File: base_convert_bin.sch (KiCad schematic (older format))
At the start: 27 parts, among them Q2 Q_PNP_BEC, Q3 Q_PNP_BEC, Q4 Q_PNP_BEC, Q5 Q_PNP_BEC, Q6 Q_NPN_BEC, Q7 Q_NPN_BEC, Q8 Q_NPN_BEC, Q9 Q_NPN_BEC

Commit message: correct LED part numbers
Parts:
- D10: Mfg Part Number 150080RS75001 -> 150080RS75000
- D11: Mfg Part Number 150080RS75002 -> 150080RS75000
- D12: Mfg Part Number 150080RS75003 -> 150080RS75000
- D13: Mfg Part Number 150080RS75004 -> 150080RS75000
- D14: Mfg Part Number 150080RS75005 -> 150080RS75000
- D15: Mfg Part Number 150080RS75006 -> 150080RS75000
- D16: Mfg Part Number 150080RS75007 -> 150080RS75000
- D2: Mfg Part Number 150080RS75008 -> 150080RS75000
- D3: Mfg Part Number 150080RS75009 -> 150080RS75000
- D4: Mfg Part Number 150080RS75010 -> 150080RS75000
- D5: Mfg Part Number 150080RS75011 -> 150080RS75000
- D6: Mfg Part Number 150080RS75012 -> 150080RS75000
- D7: Mfg Part Number 150080RS75013 -> 150080RS75000
- D8: Mfg Part Number 150080RS75014 -> 150080RS75000
- D9: Mfg Part Number 150080RS75015 -> 150080RS75000
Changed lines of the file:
@@
 F 4 "LED RED CLEAR 0805 SMD" H 5200 1750 50  0001 C CNN "Description"
 F 5 "Wurth Electronics Inc." H 5200 1750 50  0001 C CNN "Manufacture"
-F 6 "150080RS75004" H 5200 1750 50  0001 C CNN "Mfg Part Number"
+F 6 "150080RS75000" H 5200 1750 50  0001 C CNN "Mfg Part Number"
 F 7 "0805" H 5200 1750 50  0001 C CNN "Package"
 	1    5200 1550
@@
 F 4 "LED RED CLEAR 0805 SMD" H 4900 1750 50  0001 C CNN "Description"
 F 5 "Wurth Electronics Inc." H 4900 1750 50  0001 C CNN "Manufacture"
-F 6 "150080RS75015" H 4900 1750 50  0001 C CNN "Mfg Part Number"
+F 6 "150080RS75000" H 4900 1750 50  0001 C CNN "Mfg Part Number"
 F 7 "0805" H 4900 1750 50  0001 C CNN "Package"
 	1    4900 1550
@@
 F 4 "LED RED CLEAR 0805 SMD" H 4600 1750 50  0001 C CNN "Description"
 F 5 "Wurth Electronics Inc." H 4600 1750 50  0001 C CNN "Manufacture"
-F 6 "150080RS75011" H 4600 1750 50  0001 C CNN "Mfg Part Number"
+F 6 "150080RS75000" H 4600 1750 50  0001 C CNN "Mfg Part Number"
 F 7 "0805" H 4600 1750 50  0001 C CNN "Package"
 	1    4600 1550
@@
 F 4 "LED RED CLEAR 0805 SMD" H 5200 3400 50  0001 C CNN "Description"
 F 5 "Wurth Electronics Inc." H 5200 3400 50  0001 C CNN "Manufacture"
-F 6 "150080RS75005" H 5200 3400 50  0001 C CNN "Mfg Part Number"
+F 6 "150080RS75000" H 5200 3400 50  0001 C CNN "Mfg Part Number"
 F 7 "0805" H 5200 3400 50  0001 C CNN "Package"
 	1    5200 3200
@@
 F 4 "LED RED CLEAR 0805 SMD" H 4900 3400 50  0001 C CNN "Description"
 F 5 "Wurth Electronics Inc." H 4900 3400 50  0001 C CNN "Manufacture"
-F 6 "150080RS75001" H 4900 3400 50  0001 C CNN "Mfg Part Number"
+F 6 "150080RS75000" H 4900 3400 50  0001 C CNN "Mfg Part Number"
 F 7 "0805" H 4900 3400 50  0001 C CNN "Package"
 	1    4900 3200
@@
 F 4 "LED RED CLEAR 0805 SMD" H 4600 3400 50  0001 C CNN "Description"
 F 5 "Wurth Electronics Inc." H 4600 3400 50  0001 C CNN "Manufacture"
-F 6 "150080RS75012" H 4600 3400 50  0001 C CNN "Mfg Part Number"
+F 6 "150080RS75000" H 4600 3400 50  0001 C CNN "Mfg Part Number"
 F 7 "0805" H 4600 3400 50  0001 C CNN "Package"
 	1    4600 3200
@@
 F 4 "LED RED CLEAR 0805 SMD" H 4300 3400 50  0001 C CNN "Description"
 F 5 "Wurth Electronics Inc." H 4300 3400 50  0001 C CNN "Manufacture"
-F 6 "150080RS75008" H 4300 3400 50  0001 C CNN "Mfg Part Number"
+F 6 "150080RS75000" H 4300 3400 50  0001 C CNN "Mfg Part Number"
 F 7 "0805" H 4300 3400 50  0001 C CNN "Package"
 	1    4300 3200
@@
 F 4 "LED RED CLEAR 0805 SMD" H 5200 5100 50  0001 C CNN "Description"
 F 5 "Wurth Electronics Inc." H 5200 5100 50  0001 C CNN "Manufacture"
-F 6 "150080RS75006" H 5200 5100 50  0001 C CNN "Mfg Part Number"
+F 6 "150080RS75000" H 5200 5100 50  0001 C CNN "Mfg Part Number"
 F 7 "0805" H 5200 5100 50  0001 C CNN "Package"
 	1    5200 4900
@@
 F 4 "LED RED CLEAR 0805 SMD" H 4900 5100 50  0001 C CNN "Description"
 F 5 "Wurth Electronics Inc." H 4900 5100 50  0001 C CNN "Manufacture"
-F 6 "150080RS75002" H 4900 5100 50  0001 C CNN "Mfg Part Number"
+F 6 "150080RS75000" H 4900 5100 50  0001 C CNN "Mfg Part Number"
 F 7 "0805" H 4900 5100 50  0001 C CNN "Package"
 	1    4900 4900
@@
 F 4 "LED RED CLEAR 0805 SMD" H 4600 5100 50  0001 C CNN "Description"
 F 5 "Wurth Electronics Inc." H 4600 5100 50  0001 C CNN "Manufacture"
-F 6 "150080RS75013" H 4600 5100 50  0001 C CNN "Mfg Part Number"
+F 6 "150080RS75000" H 4600 5100 50  0001 C CNN "Mfg Part Number"
 F 7 "0805" H 4600 5100 50  0001 C CNN "Package"
 	1    4600 4900
@@
 F 4 "LED RED CLEAR 0805 SMD" H 4300 5100 50  0001 C CNN "Description"
 F 5 "Wurth Electronics Inc." H 4300 5100 50  0001 C CNN "Manufacture"
-F 6 "150080RS75009" H 4300 5100 50  0001 C CNN "Mfg Part Number"
+F 6 "150080RS75000" H 4300 5100 50  0001 C CNN "Mfg Part Number"
 F 7 "0805" H 4300 5100 50  0001 C CNN "Package"
 	1    4300 4900
@@
 F 4 "LED RED CLEAR 0805 SMD" H 5200 6750 50  0001 C CNN "Description"
 F 5 "Wurth Electronics Inc." H 5200 6750 50  0001 C CNN "Manufacture"
-F 6 "150080RS75007" H 5200 6750 50  0001 C CNN "Mfg Part Number"
+F 6 "150080RS75000" H 5200 6750 50  0001 C CNN "Mfg Part Number"
 F 7 "0805" H 5200 6750 50  0001 C CNN "Package"
 	1    5200 6550
@@
 F 4 "LED RED CLEAR 0805 SMD" H 4900 6750 50  0001 C CNN "Description"
 F 5 "Wurth Electronics Inc." H 4900 6750 50  0001 C CNN "Manufacture"
-F 6 "150080RS75003" H 4900 6750 50  0001 C CNN "Mfg Part Number"
+F 6 "150080RS75000" H 4900 6750 50  0001 C CNN "Mfg Part Number"
 F 7 "0805" H 4900 6750 50  0001 C CNN "Package"
 	1    4900 6550
@@
 F 4 "LED RED CLEAR 0805 SMD" H 4600 6750 50  0001 C CNN "Description"
 F 5 "Wurth Electronics Inc." H 4600 6750 50  0001 C CNN "Manufacture"
-F 6 "150080RS75014" H 4600 6750 50  0001 C CNN "Mfg Part Number"
+F 6 "150080RS75000" H 4600 6750 50  0001 C CNN "Mfg Part Number"
 F 7 "0805" H 4600 6750 50  0001 C CNN "Package"
 	1    4600 6550
@@
 F 4 "LED RED CLEAR 0805 SMD" H 4300 6750 50  0001 C CNN "Description"
 F 5 "Wurth Electronics Inc." H 4300 6750 50  0001 C CNN "Manufacture"
-F 6 "150080RS75010" H 4300 6750 50  0001 C CNN "Mfg Part Number"
+F 6 "150080RS75000" H 4300 6750 50  0001 C CNN "Mfg Part Number"
 F 7 "0805" H 4300 6750 50  0001 C CNN "Package"
 	1    4300 6550

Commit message: update RN part numbers
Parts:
- RN1, RN3: Description RES ARRAY 4 RES 4.7K OHM 1206 -> RES ARRAY 4 RES 5.6K OHM 2012; Manufacture Stackpole Electronics Inc. -> Rohm Semiconductor; Mfg Part Number RAVF164DJT4K70 -> MNR34J5ABJ562; Package 1206 -> 2012
- RN2: Mfg Part Number MNR14ERAPJ151 -> MNR34J5ABJ151; Package 1206 -> 2012
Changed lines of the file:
@@
 F 2 "Resistors_SMD:R_Array_Convex_4x1206" V 3675 1200 50  0001 C CNN
 F 3 "https://www.seielect.com/Catalog/SEI-RAVF.pdf" H 3400 1200 50  0001 C CNN
-F 4 "Stackpole Electronics Inc." H 3400 1200 60  0001 C CNN "Manufacture"
-F 5 "RAVF164DJT4K70" H 3400 1200 60  0001 C CNN "Mfg Part Number"
-F 6 "1206" H 3400 1200 60  0001 C CNN "Package"
-F 7 "RES ARRAY 4 RES 4.7K OHM 1206" H 3400 1200 60  0001 C CNN "Description"
+F 4 "Rohm Semiconductor" H 3400 1200 60  0001 C CNN "Manufacture"
+F 5 "MNR34J5ABJ562" H 3400 1200 60  0001 C CNN "Mfg Part Number"
+F 6 "2012" H 3400 1200 60  0001 C CNN "Package"
+F 7 "RES ARRAY 4 RES 5.6K OHM 2012" H 3400 1200 60  0001 C CNN "Description"
 	1    3400 1200
 	0    -1   1    0
@@
 F 2 "Resistors_SMD:R_Array_Convex_4x1206" V 10675 2350 50  0001 C CNN
 F 3 "https://www.seielect.com/Catalog/SEI-RAVF.pdf" H 10400 2350 50  0001 C CNN
-F 4 "Stackpole Electronics Inc." H 10400 2350 60  0001 C CNN "Manufacture"
-F 5 "RAVF164DJT4K70" H 10400 2350 60  0001 C CNN "Mfg Part Number"
-F 6 "1206" H 10400 2350 60  0001 C CNN "Package"
-F 7 "RES ARRAY 4 RES 4.7K OHM 1206" H 10400 2350 60  0001 C CNN "Description"
+F 4 "Rohm Semiconductor" H 10400 2350 60  0001 C CNN "Manufacture"
+F 5 "MNR34J5ABJ562" H 10400 2350 60  0001 C CNN "Mfg Part Number"
+F 6 "2012" H 10400 2350 60  0001 C CNN "Package"
+F 7 "RES ARRAY 4 RES 5.6K OHM 2012" H 10400 2350 60  0001 C CNN "Description"
 	1    10400 2350
 	0    1    1    0
@@
 F 3 "http://rohmfs.rohm.com/en/products/databook/datasheet/passive/resistor/chip_resistor_network/mnr_g.pdf" H 8200 1700 50  0001 C CNN
 F 4 "Rohm Semiconductor" H 8200 1700 60  0001 C CNN "Manufacture"
-F 5 "MNR14ERAPJ151" H 8200 1700 60  0001 C CNN "Mfg Part Number"
-F 6 "1206" H 8200 1700 60  0001 C CNN "Package"
+F 5 "MNR34J5ABJ151" H 8200 1700 60  0001 C CNN "Mfg Part Number"
+F 6 "2012" H 8200 1700 60  0001 C CNN "Package"
 F 7 "RES ARRAY 4 RES 150 OHM 1206" H 8200 1700 60  0001 C CNN "Description"
 	1    8200 1700

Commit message: PNP transistor change to prebiased PNP
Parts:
- Q2: Description TRANS PNP 40V 0.2A SOT23 -> TRANS PREBIAS PNP 250MW TO236AB; Mfg Part Number PMBT3906,235 -> PDTA123ET,215
- Q3: Description TRANS PNP 40V 0.2A SOT24 -> TRANS PREBIAS PNP 250MW TO236AB; Mfg Part Number PMBT3906,235 -> PDTA123ET,215
- Q4: Description TRANS PNP 40V 0.2A SOT26 -> TRANS PREBIAS PNP 250MW TO236AB; Mfg Part Number PMBT3906,235 -> PDTA123ET,215
- Q5: Description TRANS PNP 40V 0.2A SOT27 -> TRANS PREBIAS PNP 250MW TO236AB; Mfg Part Number PMBT3906,235 -> PDTA123ET,215
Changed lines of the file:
@@
 F 1 "Q_PNP_BEC" H 4400 950 50  0000 L CNN
 F 2 "TO_SOT_Packages_SMD:SOT-23" H 4400 1100 50  0001 C CNN
-F 3 "https://assets.nexperia.com/documents/data-sheet/PMBT3906.pdf" H 4200 1000 50  0001 C CNN
-F 4 "TRANS PNP 40V 0.2A SOT23" H 4400 1150 50  0001 C CNN "Description"
+F 3 "https://assets.nexperia.com/documents/data-sheet/PDTA123E_SERIES.pdf" H 4200 1000 50  0001 C CNN
+F 4 "TRANS PREBIAS PNP 250MW TO236AB" H 4400 1150 50  0001 C CNN "Description"
 F 5 "Nexperia USA Inc." H 4400 1150 50  0001 C CNN "Manufacture"
-F 6 "PMBT3906,235" H 4400 1150 50  0001 C CNN "Mfg Part Number"
+F 6 "PDTA123ET,215" H 4400 1150 50  0001 C CNN "Mfg Part Number"
 F 7 "SOT-23" H 4400 1150 50  0001 C CNN "Package"
 	1    4200 1000
@@
 F 1 "Q_PNP_BEC" H 4400 2600 50  0000 L CNN
 F 2 "TO_SOT_Packages_SMD:SOT-23" H 4400 2750 50  0001 C CNN
-F 3 "https://assets.nexperia.com/documents/data-sheet/PMBT3906.pdf" H 4200 2650 50  0001 C CNN
-F 4 "TRANS PNP 40V 0.2A SOT24" H 4400 2800 50  0001 C CNN "Description"
+F 3 "https://assets.nexperia.com/documents/data-sheet/PDTA123E_SERIES.pdf" H 4200 2650 50  0001 C CNN
+F 4 "TRANS PREBIAS PNP 250MW TO236AB" H 4400 2800 50  0001 C CNN "Description"
 F 5 "Nexperia USA Inc." H 4400 2800 50  0001 C CNN "Manufacture"
-F 6 "PMBT3906,235" H 4400 2800 50  0001 C CNN "Mfg Part Number"
+F 6 "PDTA123ET,215" H 4400 2800 50  0001 C CNN "Mfg Part Number"
 F 7 "SOT-23" H 4400 2800 50  0001 C CNN "Package"
 	1    4200 2650
@@
 F 1 "Q_PNP_BEC" H 4400 4300 50  0000 L CNN
 F 2 "TO_SOT_Packages_SMD:SOT-23" H 4400 4450 50  0001 C CNN
-F 3 "https://assets.nexperia.com/documents/data-sheet/PMBT3906.pdf" H 4200 4350 50  0001 C CNN
-F 4 "TRANS PNP 40V 0.2A SOT26" H 4400 4500 50  0001 C CNN "Description"
+F 3 "https://assets.nexperia.com/documents/data-sheet/PDTA123E_SERIES.pdf" H 4200 4350 50  0001 C CNN
+F 4 "TRANS PREBIAS PNP 250MW TO236AB" H 4400 4500 50  0001 C CNN "Description"
 F 5 "Nexperia USA Inc." H 4400 4500 50  0001 C CNN "Manufacture"
-F 6 "PMBT3906,235" H 4400 4500 50  0001 C CNN "Mfg Part Number"
+F 6 "PDTA123ET,215" H 4400 4500 50  0001 C CNN "Mfg Part Number"
 F 7 "SOT-23" H 4400 4500 50  0001 C CNN "Package"
 	1    4200 4350
@@
 F 1 "Q_PNP_BEC" H 4400 5950 50  0000 L CNN
 F 2 "TO_SOT_Packages_SMD:SOT-23" H 4400 6100 50  0001 C CNN
-F 3 "https://assets.nexperia.com/documents/data-sheet/PMBT3906.pdf" H 4200 6000 50  0001 C CNN
-F 4 "TRANS PNP 40V 0.2A SOT27" H 4400 6150 50  0001 C CNN "Description"
+F 3 "https://assets.nexperia.com/documents/data-sheet/PDTA123E_SERIES.pdf" H 4200 6000 50  0001 C CNN
+F 4 "TRANS PREBIAS PNP 250MW TO236AB" H 4400 6150 50  0001 C CNN "Description"
 F 5 "Nexperia USA Inc." H 4400 6150 50  0001 C CNN "Manufacture"
-F 6 "PMBT3906,235" H 4400 6150 50  0001 C CNN "Mfg Part Number"
+F 6 "PDTA123ET,215" H 4400 6150 50  0001 C CNN "Mfg Part Number"
 F 7 "SOT-23" H 4400 6150 50  0001 C CNN "Package"
 	1    4200 6000
@@
 	4300 750  4300 800
 Wire Wire Line
-	4300 1200 4300 1400
+	4300 1200 4300 1300
 Wire Wire Line
 	5200 1300 5200 1400
 Wire Wire Line
-	4300 1300 5200 1300
+	4300 1300 4600 1300
 Wire Wire Line
 	4900 1400 4900 1300
@@
 Wire Wire Line
 	5200 1950 5200 1700
-Wire Bus Line
-	4400 2050 5400 2050
 Wire Wire Line
 	9750 2150 10200 2150
@@
 	4300 2400 4300 2450
 Wire Wire Line
-	4300 2850 4300 3050
+	4300 2850 4300 2950
 Wire Wire Line
 	5200 2950 5200 3050
 Wire Wire Line
-	4300 2950 5200 2950
+	4300 2950 4600 2950
 Wire Wire Line
 	4900 3050 4900 2950
@@
 Wire Wire Line
 	5200 3600 5200 3350
-Wire Bus Line
-	4400 3700 5400 3700
 Wire Wire Line
 	4300 4100 4300 4150
 Wire Wire Line
-	4300 4550 4300 4750
+	4300 4550 4300 4650
 Wire Wire Line
 	5200 4650 5200 4750
 Wire Wire Line
-	4300 4650 5200 4650
+	4300 4650 4600 4650
 Wire Wire Line
 	4900 4750 4900 4650
@@
 Wire Wire Line
 	5200 5300 5200 5050
-Wire Bus Line
-	4400 5400 5400 5400
 Wire Wire Line
 	4300 5750 4300 5800
 Wire Wire Line
-	4300 6200 4300 6400
+	4300 6200 4300 6300
 Wire Wire Line
 	5200 6300 5200 6400
 Wire Wire Line
-	4300 6300 5200 6300
+	4300 6300 4600 6300
 Wire Wire Line
 	4900 6400 4900 6300
@@
 Wire Wire Line
 	5200 6950 5200 6700
-Wire Bus Line
-	4400 7050 5400 7050
 Wire Wire Line
 	8000 1500 7700 1500
@@
 	8000 1800 7700 1800
 Wire Bus Line
-	7600 1000 7600 1700
-Wire Bus Line
 	7600 1000 5500 1000
-Wire Bus Line
-	5500 1000 5500 6950
 Entry Wire Line
 	4300 1950 4400 2050
@@
 Wire Wire Line
 	8700 5850 9450 5850
+Wire Wire Line
+	4300 1300 4300 1400
+Wire Wire Line
+	4900 1300 5200 1300
+Wire Wire Line
+	4600 1300 4900 1300
+Wire Wire Line
+	4300 2950 4300 3050
+Wire Wire Line
+	4900 2950 5200 2950
+Wire Wire Line
+	4600 2950 4900 2950
+Wire Wire Line
+	4300 4650 4300 4750
+Wire Wire Line
+	4900 4650 5200 4650
+Wire Wire Line
+	4600 4650 4900 4650
+Wire Wire Line
+	4300 6300 4300 6400
+Wire Wire Line
+	4900 6300 5200 6300
+Wire Wire Line
+	4600 6300 4900 6300
+Wire Bus Line
+	4400 2050 5400 2050
+Wire Bus Line
+	4400 3700 5400 3700
+Wire Bus Line
+	4400 5400 5400 5400
+Wire Bus Line
+	4400 7050 5400 7050
+Wire Bus Line
+	7600 1000 7600 1700
+Wire Bus Line
+	5500 1000 5500 6950
 $EndSCHEMATC

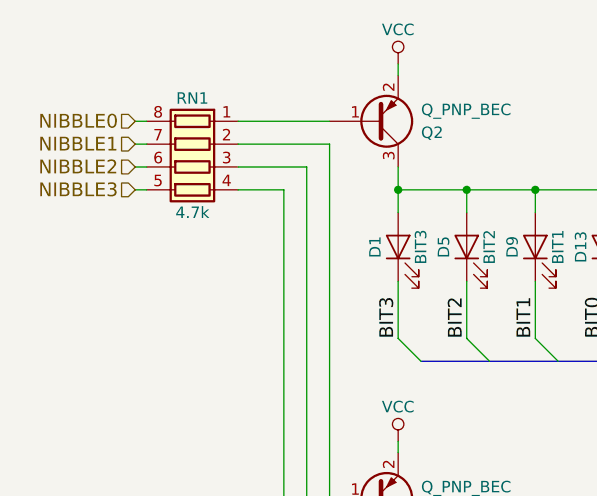
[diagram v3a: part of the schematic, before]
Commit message: PNP base resistor network change to 10k
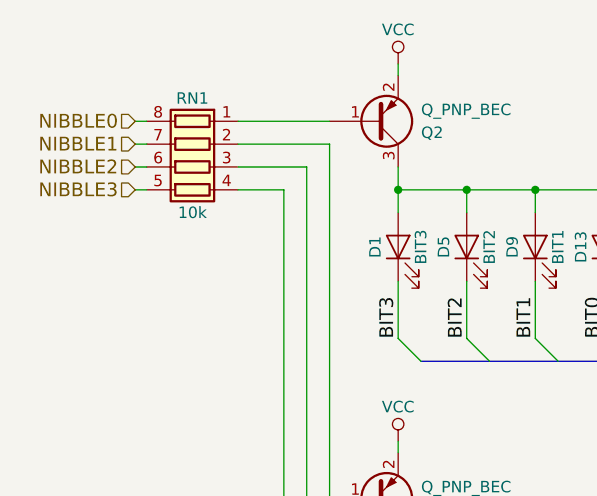
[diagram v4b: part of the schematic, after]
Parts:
- RN1: value 4.7k -> 10k; Description RES ARRAY 4 RES 5.6K OHM 2012 -> RES ARRAY 4 RES 10K OHM 2012; Manufacture Rohm Semiconductor -> Yageo; Mfg Part Number MNR34J5ABJ562 -> YC324-JK-0710KL
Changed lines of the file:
@@
 P 3400 1200
 F 0 "RN1" V 3100 1200 50  0000 C CNN
-F 1 "4.7k" V 3600 1200 50  0000 C CNN
+F 1 "10k" V 3600 1200 50  0000 C CNN
 F 2 "Resistors_SMD:R_Array_Convex_4x1206" V 3675 1200 50  0001 C CNN
-F 3 "https://www.seielect.com/Catalog/SEI-RAVF.pdf" H 3400 1200 50  0001 C CNN
-F 4 "Rohm Semiconductor" H 3400 1200 60  0001 C CNN "Manufacture"
-F 5 "MNR34J5ABJ562" H 3400 1200 60  0001 C CNN "Mfg Part Number"
+F 3 "https://media.digikey.com/pdf/Data%20Sheets/Yageo%20PDFs/YC102-358,TC122-164_Series_DS.pdf" H 3400 1200 50  0001 C CNN
+F 4 "Yageo" H 3400 1200 60  0001 C CNN "Manufacture"
+F 5 "YC324-JK-0710KL" H 3400 1200 60  0001 C CNN "Mfg Part Number"
 F 6 "2012" H 3400 1200 60  0001 C CNN "Package"
-F 7 "RES ARRAY 4 RES 5.6K OHM 2012" H 3400 1200 60  0001 C CNN "Description"
+F 7 "RES ARRAY 4 RES 10K OHM 2012" H 3400 1200 60  0001 C CNN "Description"
 	1    3400 1200
 	0    -1   1    0
